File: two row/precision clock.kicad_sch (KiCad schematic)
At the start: 52 parts, among them P1 USB_C_Plug_USB2.0, P2 USB_C_Plug_USB2.0, Q1 MMBT3906, Q2 MMBT3906

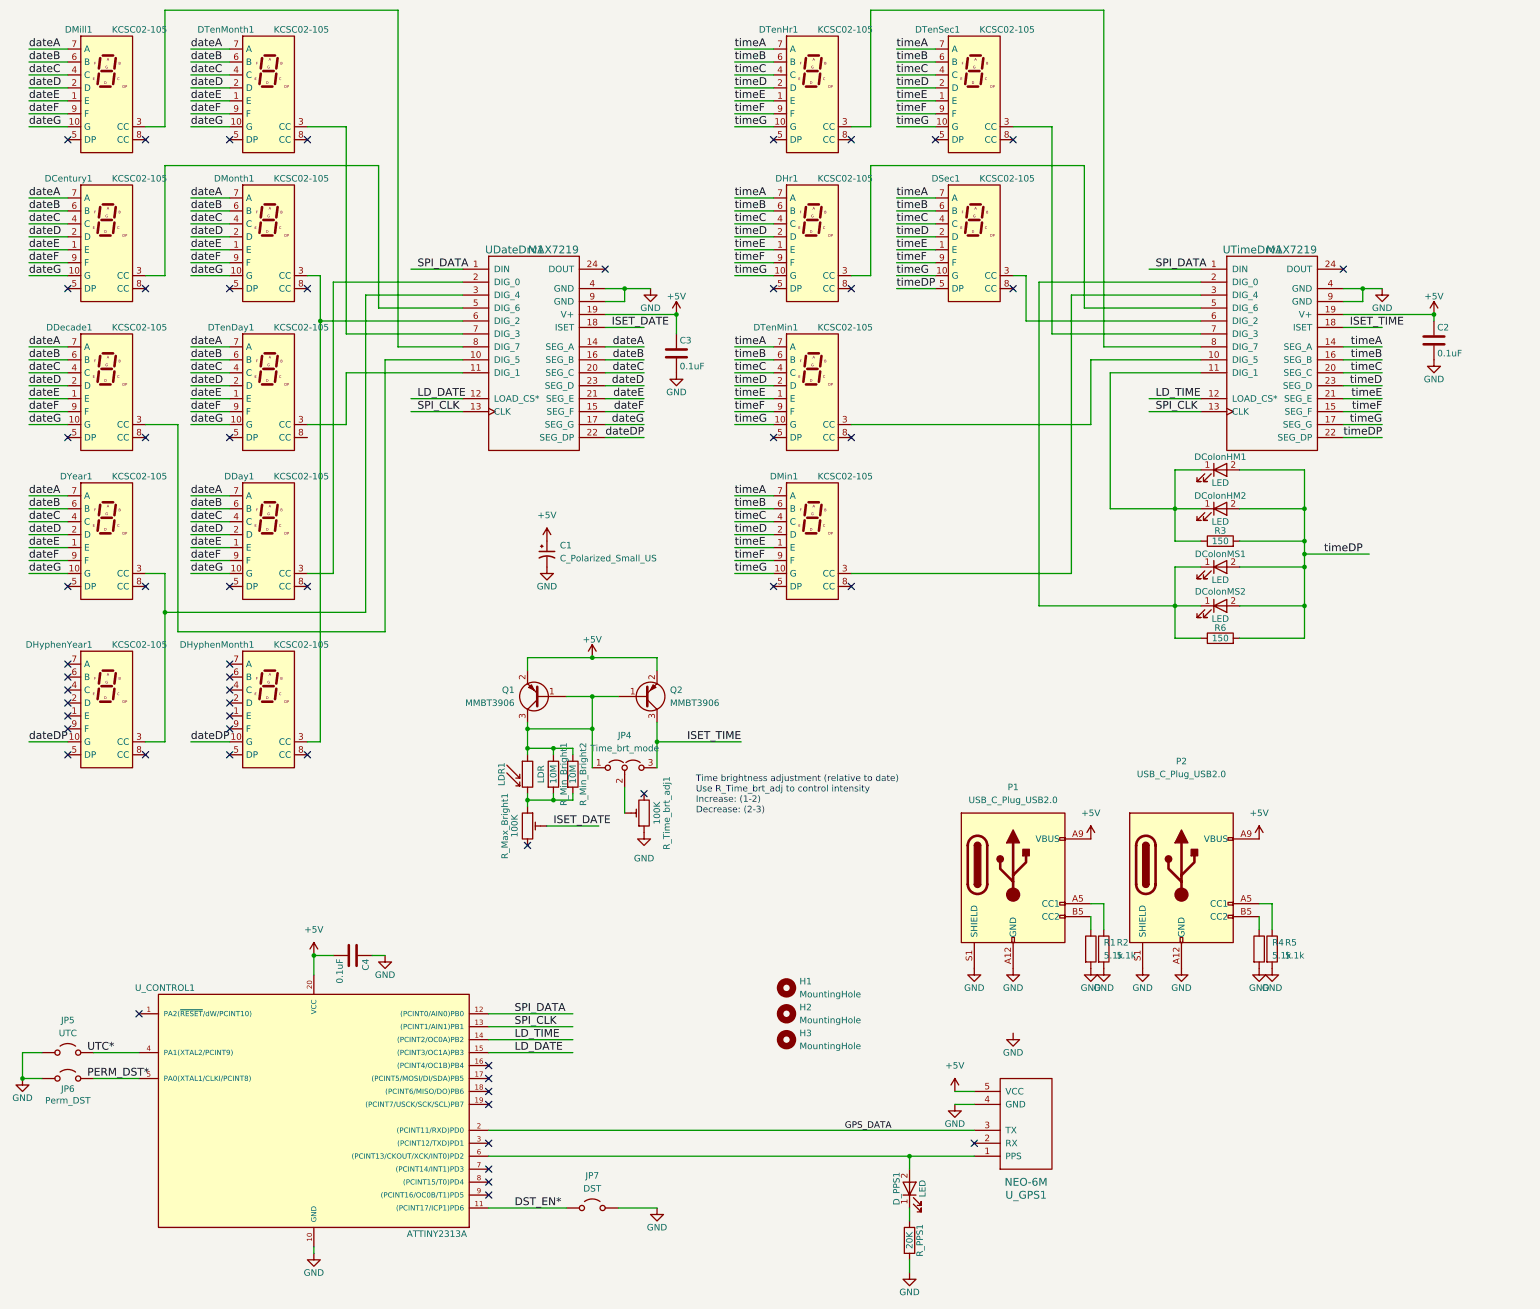
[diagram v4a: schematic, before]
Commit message: Fix reference designators
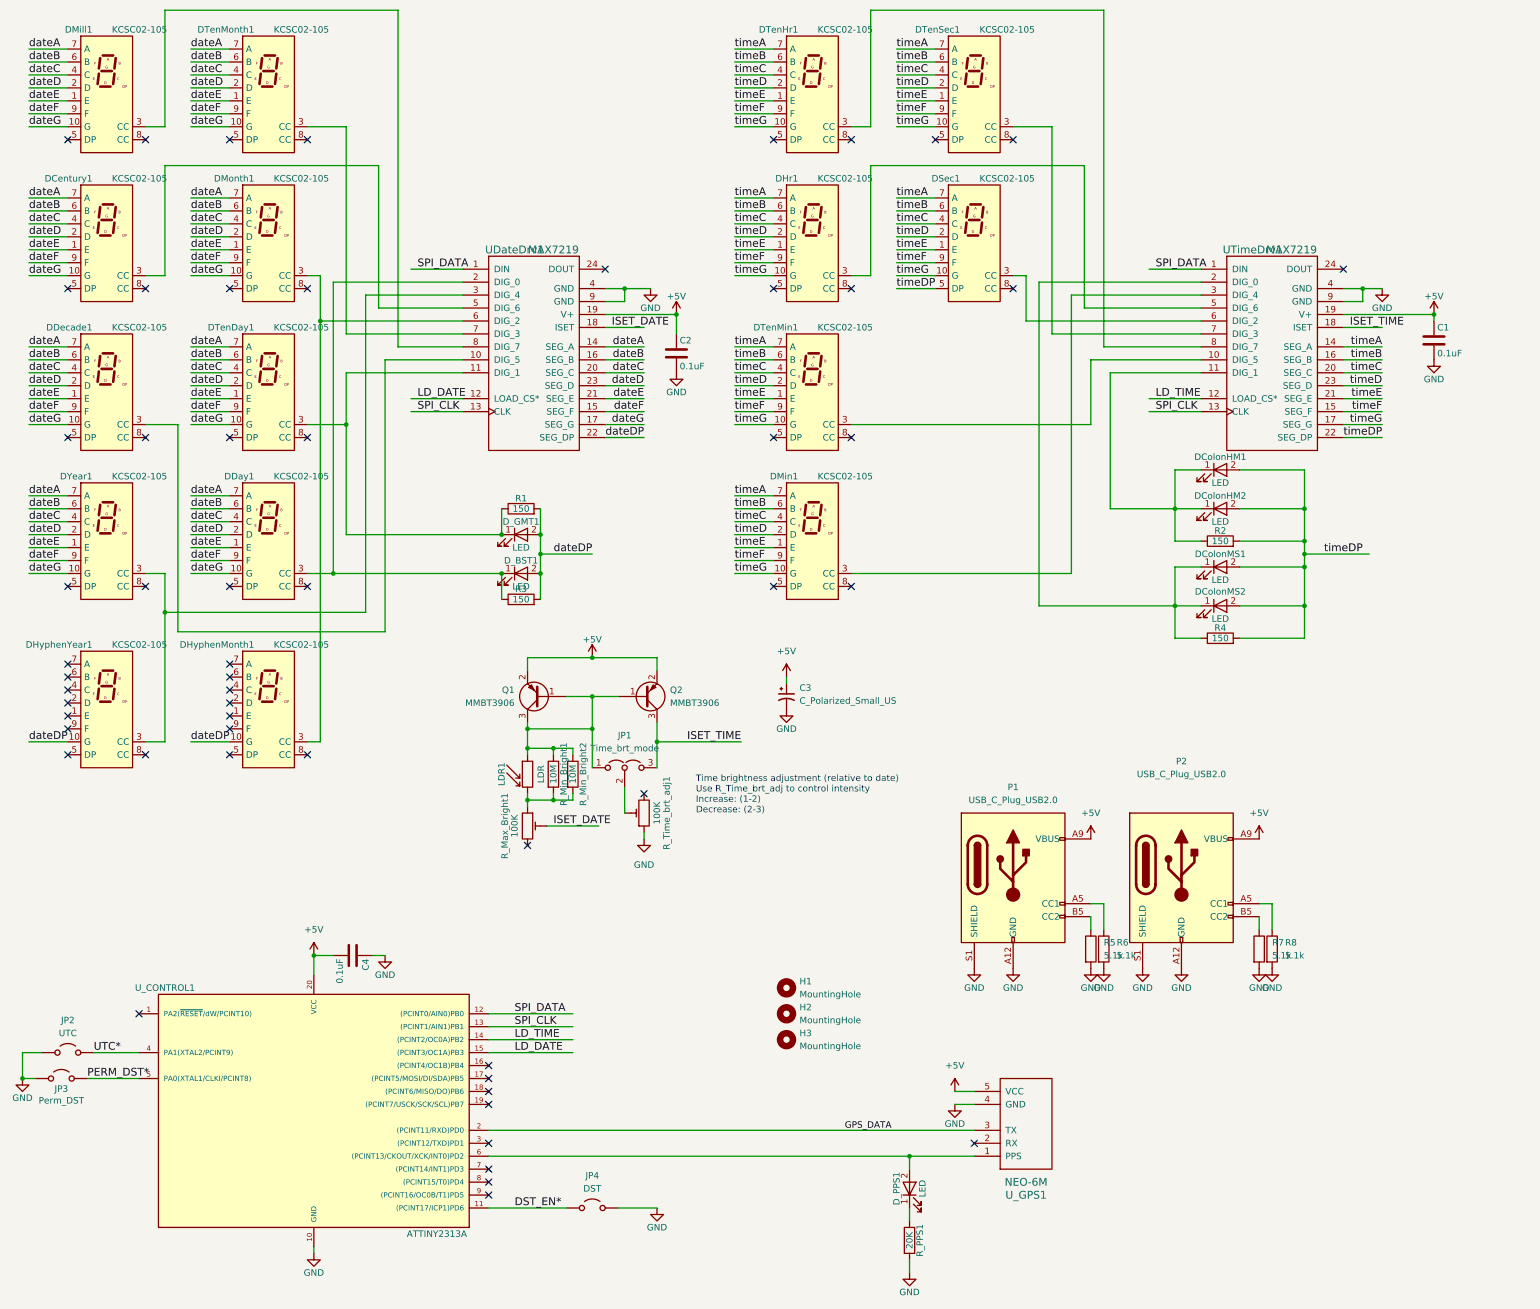
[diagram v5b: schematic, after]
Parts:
- added D_BST1, D_GMT1: LED, LED_SMD:LED_1206_3216Metric, symbol precision-clock-rescue:LED
- added R1, R3: 150, Resistor_SMD:R_1206_3216Metric, symbol precision-clock-rescue:R
- renumbered C2 to C1, C3 to C2, C1 to C3, JP4 to JP1, JP5 to JP2, JP6 to JP3, JP7 to JP4, R3 to R2, R6 to R4, R1 to R5, R2 to R6, R4 to R7, R5 to R8
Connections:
- net PERM_DST*: now also JP3.1 (A), U_CONTROL1.5 (PA0(XTAL1/CLKI/PCINT8))
- net UTC*: now also JP2.1 (A), U_CONTROL1.4 (PA1(XTAL2/PCINT9))
- net dateDP: now also D_BST1.2 (A), D_GMT1.2 (A), R1.2, R3.2
- net at DTenDay1.3 (CC), UDateDrv1.11 (DIG_1): now also D_GMT1.1 (K), R1.1
- net at DDay1.3 (CC), UDateDrv1.2 (DIG_0): now also D_BST1.1 (K), R3.1
- no-connect marks 56 -> 57
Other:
- moved on the sheet: C3, JP3
